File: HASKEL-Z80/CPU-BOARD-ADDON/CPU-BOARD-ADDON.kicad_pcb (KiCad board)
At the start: 2 copper layers, 115 x 160.3 mm, 51 parts, among them J101 conn_Y7, J102 Conn_Selector, J103 Conn_Enh, J104 Conn_RC2014, SW101 SW_Push, SW102 SW_Push, SW103 SW_Push, SW104 SW_Push, SW105 SW_Push, SW106 SW_Push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

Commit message: update projects
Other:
- board text added: "r2"
- board text removed: "r1"

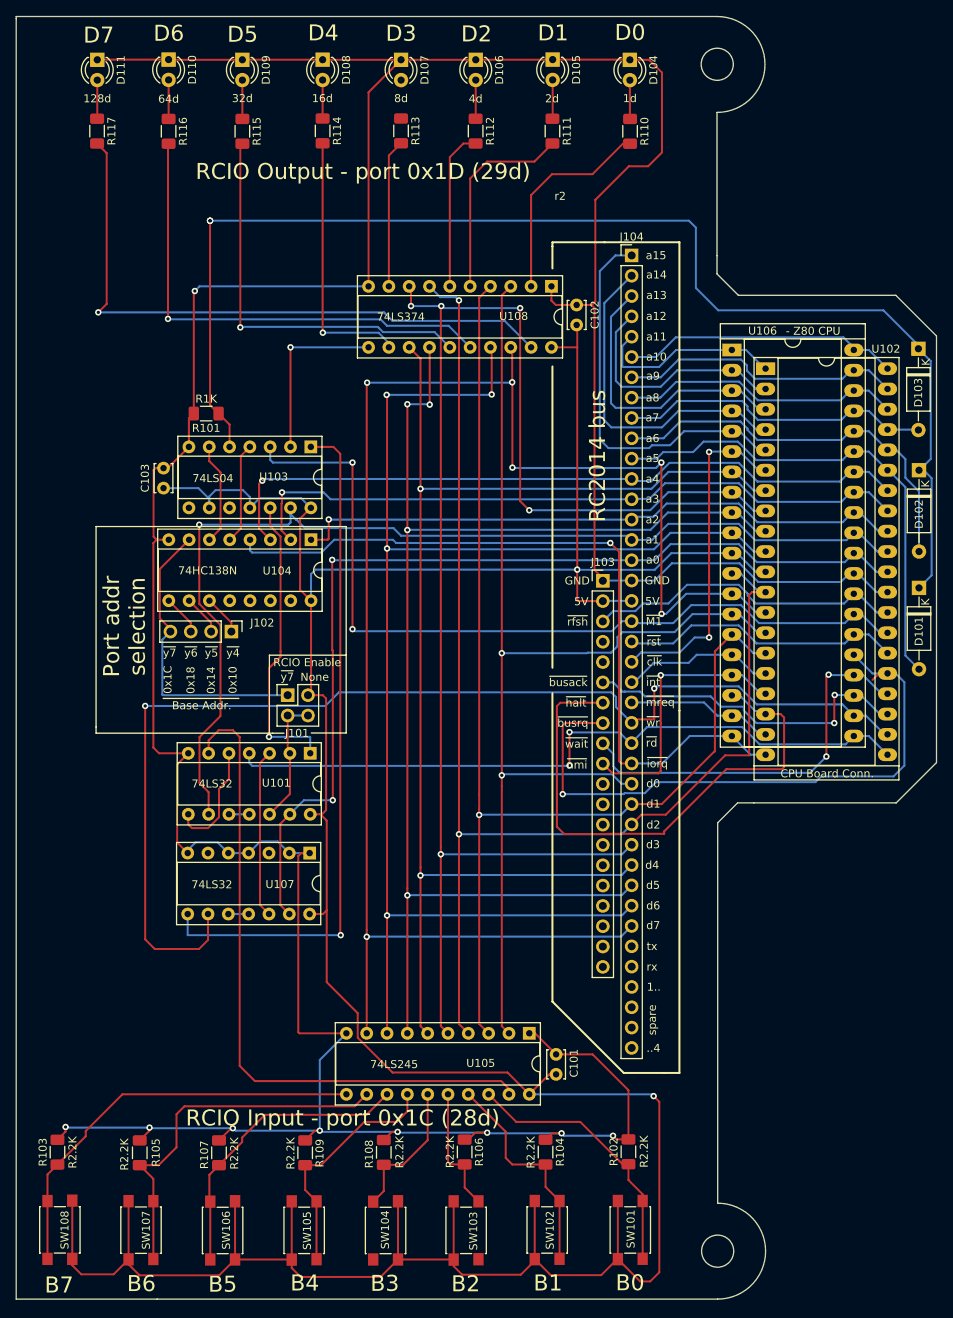
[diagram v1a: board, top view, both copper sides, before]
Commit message: First assembly example with CPU-BOARD-AddOn
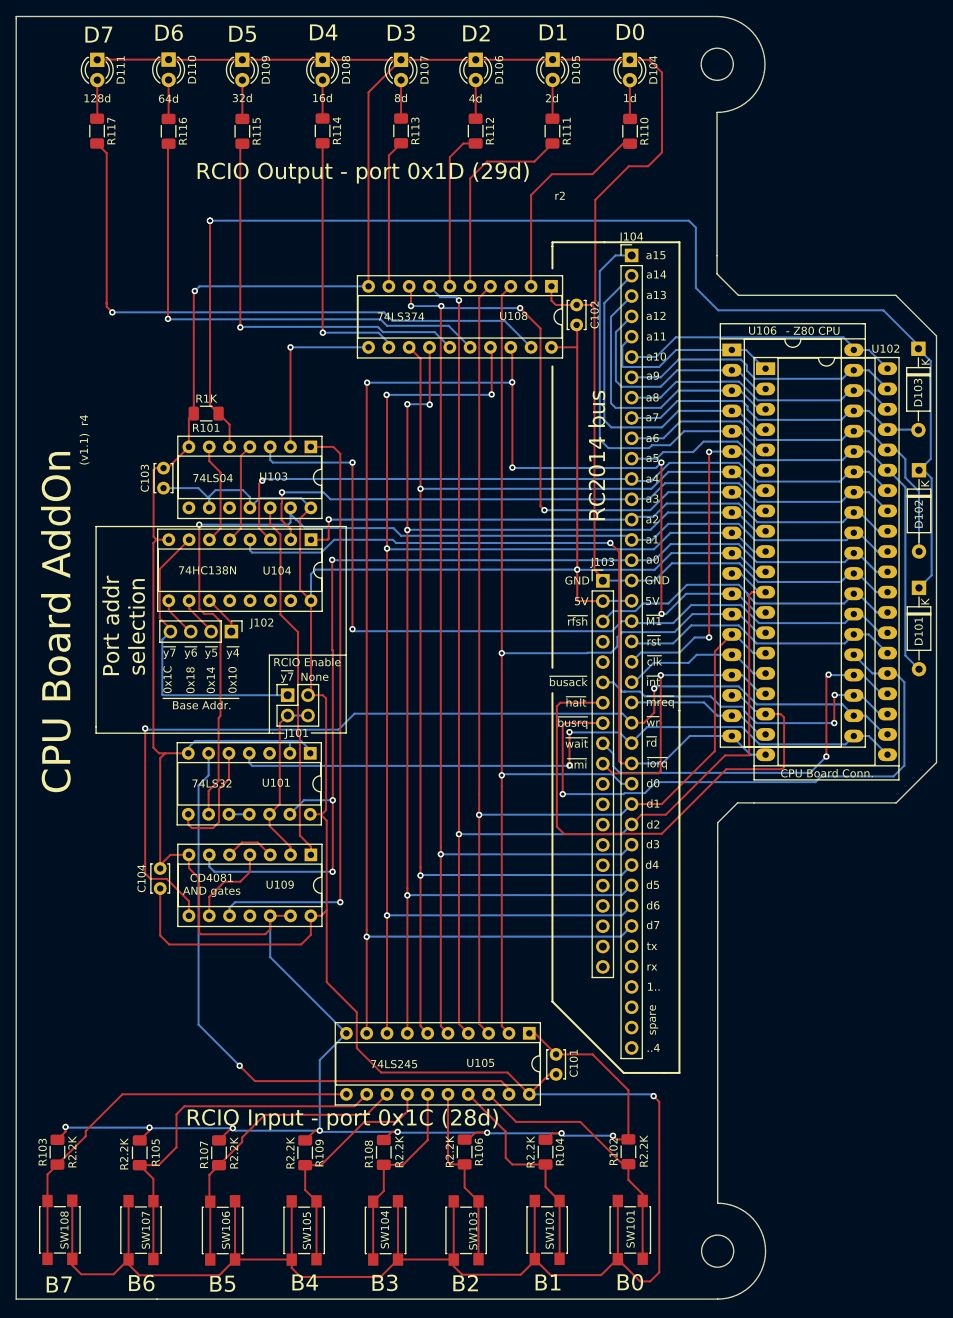
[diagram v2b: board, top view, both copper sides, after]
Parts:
- removed U107: 74LS32, Package_DIP:DIP-14_W7.62mm_Socket
- added C104: C10nF, Capacitor_THT:C_Disc_D3.4mm_W2.1mm_P2.50mm, F.Cu at (69.0, 134.0)
- added U109: 4081, Package_DIP:DIP-14_W7.62mm_Socket, F.Cu at (87.8, 129.8)
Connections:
- U101 pad 1: Net-(U101-Pad1) -> GND
- U101 pad 2: _RCIOce -> GND
- U103 pad 12: Net-(U101-Pad1) -> Net-(U103-Pad12)
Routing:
- net Net-(U103-Pad12): track 0.00 -> 45.5 mm
- net Net-(U101-Pad1): track 36.9 -> 0.00 mm, vias 1 -> 0
- net +5V: track 417.0 -> 445.9 mm
- net Net-(U101-Pad3): track 21.1 -> 0.00 mm
- net GND: track 488.5 -> 508.1 mm
- net /_wr: track 143.7 -> 127.2 mm
- net /a0: track 122.2 -> 134.9 mm, vias 2 -> 3
- net Net-(U109-Pad4): track 0.00 -> 10.9 mm
- net Net-(U103-Pad1): track 86.0 -> 75.2 mm
- net Net-(R108-Pad2): track 17.7 -> 24.9 mm
- net Net-(R106-Pad2): track 16.0 -> 23.2 mm
- net Net-(U109-Pad3): track 0.00 -> 6.36 mm
- net _RCIOce: track 16.1 -> 22.0 mm
- net Net-(U101-Pad6): track 83.0 -> 77.2 mm, vias 0 -> 1
- net Net-(D107-Pad2): track 0.00 -> 4.80 mm
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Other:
- board text added: "(v1.1) r4"
- board text added: "CD4081 AND gates"
- board text added: "CPU Board AddOn"
